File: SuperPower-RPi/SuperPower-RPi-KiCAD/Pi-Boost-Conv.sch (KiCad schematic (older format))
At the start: 22 parts, among them U1 TPS61088

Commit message: Part Meta-data updates continued.
(cherry picked from commit d0ad2c93dfb1e315a7dc98683a53ed7dcb5f49ff)
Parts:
- U1: Digi-Key PN (none) -> 296-43620-1-ND; Mfg (none) -> Texas Instruments; Mfg PN (none) -> TPS61088RHLR
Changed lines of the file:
@@
 F 2 "" H 5550 3250 50  0001 C CNN
 F 3 "https://www.ti.com/lit/ds/symlink/tps61088.pdf?ts=1601341027862" H 5550 3250 50  0001 C CNN
+F 4 "296-43620-1-ND" H 5450 3900 50  0001 C CNN "Digi-Key PN"
+F 5 "Texas Instruments" H 5450 3900 50  0001 C CNN "Mfg"
+F 6 "TPS61088RHLR" H 5450 3900 50  0001 C CNN "Mfg PN"
 	1    5450 3900
 	1    0    0    -1

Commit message: Added local footprint library, and associated components.
(cherry picked from commit 78b1abfd5fe55b90039e798d35239acda24b0417)
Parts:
- C13: footprint (none) -> Capacitor_SMD:C_0603_1608Metric
- L1: Mfg (none) -> FIX FOOTPRINT
- R4: footprint (none) -> Resistor_SMD:R_0603_1608Metric
- U1: footprint (none) -> SuperPower-RPi-KiCAD:TI_VQFN_3.5x4.5mm
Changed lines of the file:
@@
 F 2 "" H 3900 3400 50  0001 C CNN
 F 3 "~" H 3900 3400 50  0001 C CNN
+F 4 "FIX FOOTPRINT" H 3900 3400 50  0001 C CNN "Mfg"
 	1    3900 3400
 	0    -1   -1   0
@@
 F 0 "R4" H 7100 4250 50  0000 C CNN
 F 1 "R" H 7100 4350 50  0000 C CNN
-F 2 "" V 6930 4300 50  0001 C CNN
+F 2 "Resistor_SMD:R_0603_1608Metric" V 6930 4300 50  0001 C CNN
 F 3 "~" H 7000 4300 50  0001 C CNN
 	1    7000 4300
@@
 F 0 "C13" H 6800 4700 50  0000 C CNN
 F 1 "C" H 6850 4800 50  0000 C CNN
-F 2 "" H 7038 4550 50  0001 C CNN
+F 2 "Capacitor_SMD:C_0603_1608Metric" H 7038 4550 50  0001 C CNN
 F 3 "~" H 7000 4700 50  0001 C CNN
 	1    7000 4700
@@
 F 0 "U1" H 5475 3827 50  0000 C CNN
 F 1 "TPS61088" H 5475 3736 50  0000 C CNN
-F 2 "" H 5550 3250 50  0001 C CNN
+F 2 "SuperPower-RPi-KiCAD:TI_VQFN_3.5x4.5mm" H 5550 3250 50  0001 C CNN
 F 3 "https://www.ti.com/lit/ds/symlink/tps61088.pdf?ts=1601341027862" H 5550 3250 50  0001 C CNN
 F 4 "296-43620-1-ND" H 5450 3900 50  0001 C CNN "Digi-Key PN"

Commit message: Added temporary footprints and imported into pcb.
(cherry picked from commit a685dfc635e321a03e1c1fd194e70e2193ef2183)
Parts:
- L1: footprint (none) -> Inductor_SMD:L_Vishay_IHLP-2525
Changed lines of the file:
@@
 F 0 "L1" V 4090 3400 50  0000 C CNN
 F 1 "4.7uH" V 3999 3400 50  0000 C CNN
-F 2 "" H 3900 3400 50  0001 C CNN
+F 2 "Inductor_SMD:L_Vishay_IHLP-2525" H 3900 3400 50  0001 C CNN
 F 3 "~" H 3900 3400 50  0001 C CNN
 F 4 "FIX FOOTPRINT" H 3900 3400 50  0001 C CNN "Mfg"

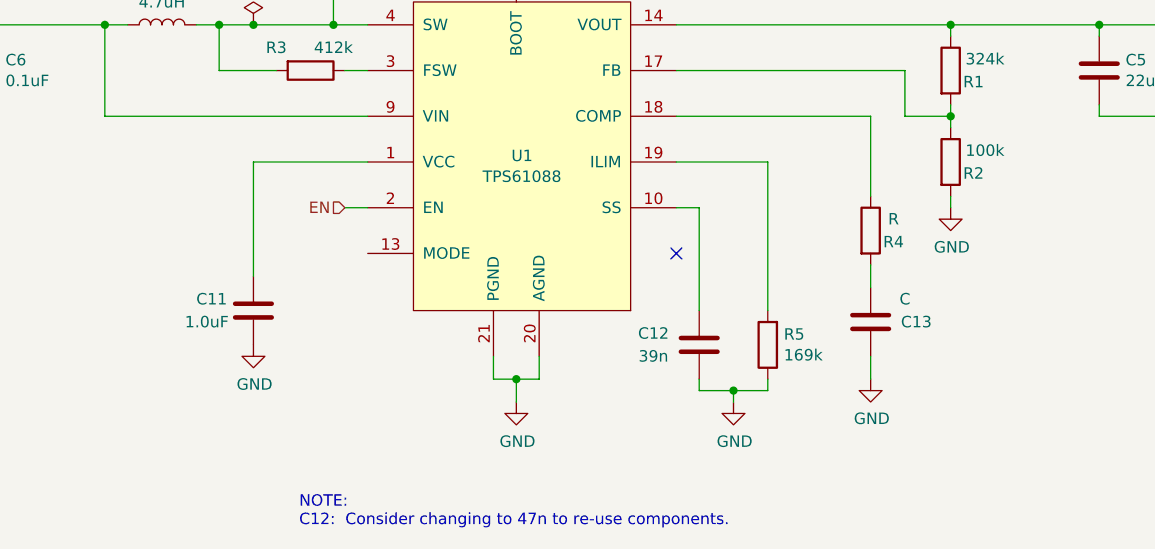
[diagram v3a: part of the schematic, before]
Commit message: PCB Updates.
Added new components, and did some arranging.
Updates TPS61088 and bq25895 footprints to use 0.3mm vias.  PCBWay's minimum via size is 0.3mm.
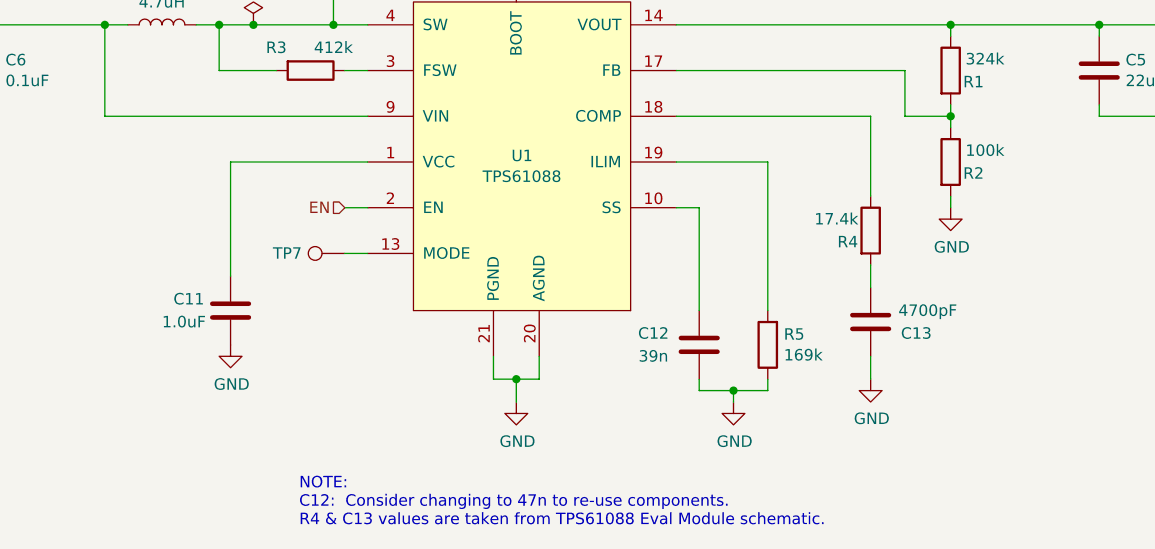
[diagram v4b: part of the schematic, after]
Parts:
- added TP7: DNP, TestPoint:TestPoint_Pad_1.0x1.0mm, symbol Connector:TestPoint
- C13: value C -> 4700pF
- R4: value R -> 17.4k
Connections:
- net at U1.13 (MODE): now also TP7.1
- no-connect marks 1 -> 0
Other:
- note added: "NOTE:\nC12: Consider changing to 47n to re-use components.\nR4 & C13 values are taken from TPS61088 Eval Module schematic."
- note removed: "NOTE:\nC12: Consider changing to 47n to re-use components."
- moved on the sheet: C11

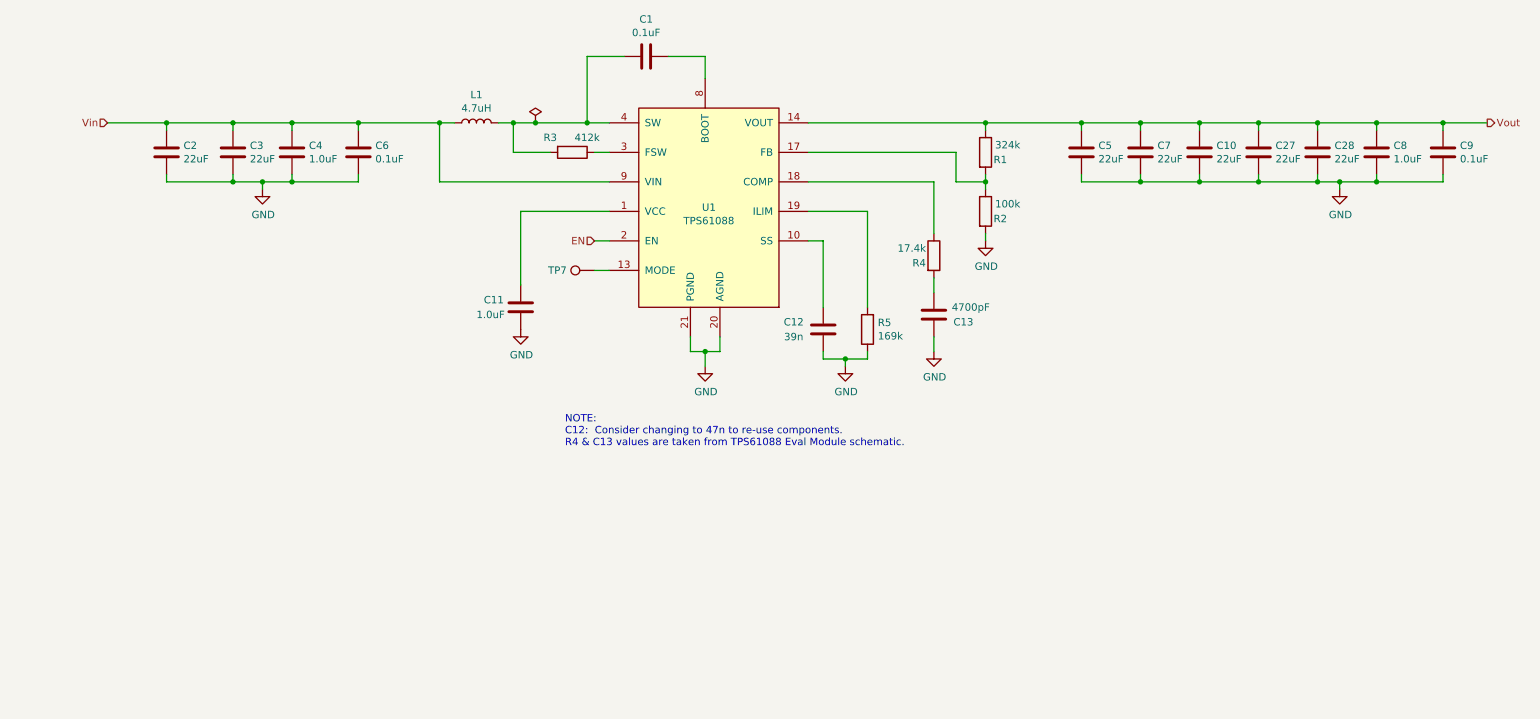
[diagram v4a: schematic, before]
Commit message: Changed Boost Converter passives to the values included in the eval kit.
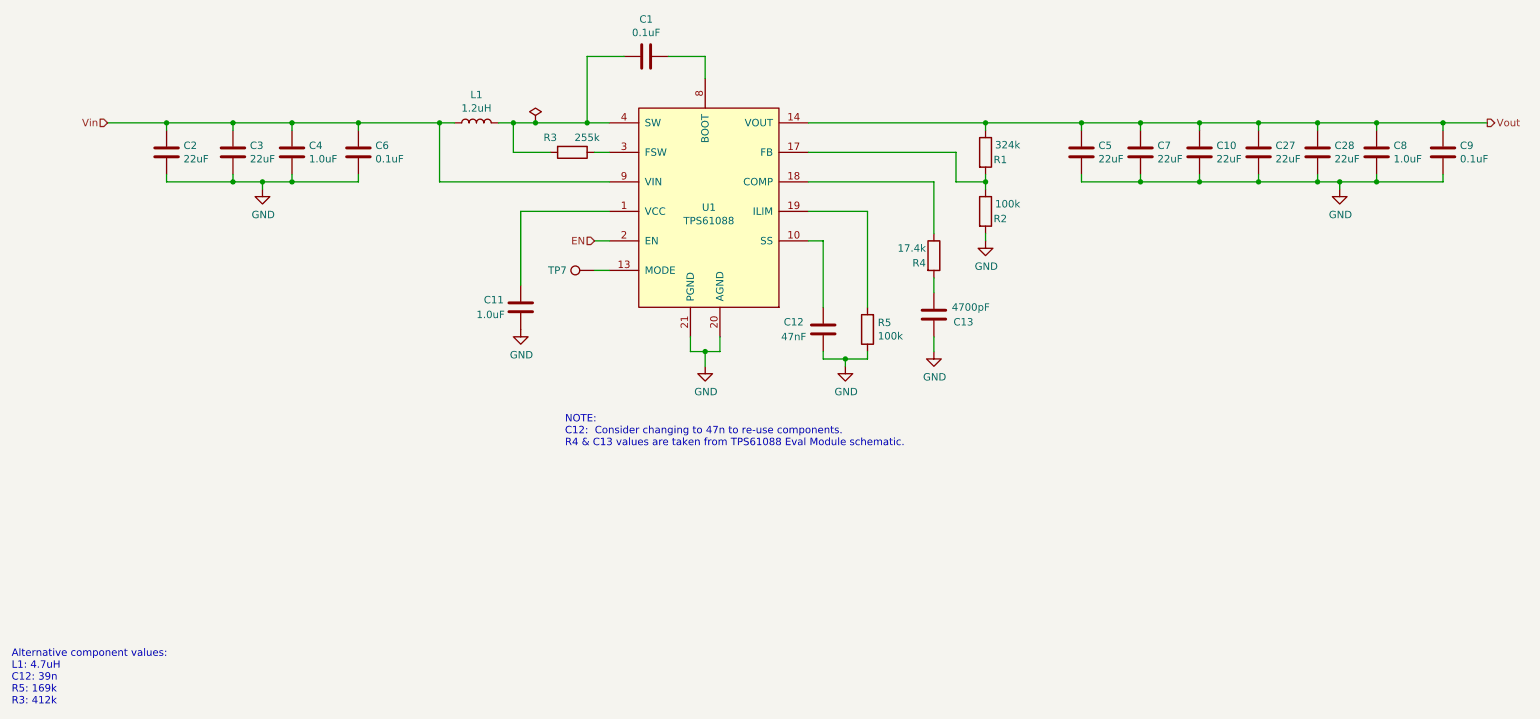
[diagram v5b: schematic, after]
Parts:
- C12: value 39n -> 47nF; footprint Capacitor_SMD:C_0603_1608Metric -> Capacitor_SMD:C_0402_1005Metric; Digi-Key PN (none) -> 490-3254-1-ND; Mfg (none) -> Murata; Mfg PN (none) -> GRM155R71E473KA88D
- C13: footprint Capacitor_SMD:C_0603_1608Metric -> Capacitor_SMD:C_0402_1005Metric
- L1: value 4.7uH -> 1.2uH; footprint Inductor_SMD:L_Vishay_IHLP-2525 -> SuperPower-RPi-KiCAD:L_Sumida_CDMC8D28_9.5x8.7mm; Digi-Key PN (none) -> 308-1618-1-ND; Mfg FIX FOOTPRINT -> Sumida; Mfg PN (none) -> CDMC8D28NP-1R2MC
- R1: footprint Resistor_SMD:R_0603_1608Metric -> Resistor_SMD:R_0402_1005Metric
- R2: footprint Resistor_SMD:R_0603_1608Metric -> Resistor_SMD:R_0402_1005Metric; Digi-Key PN 311-100KHRCT-ND -> (none); Mfg Yageo -> (none); Mfg PN RC0603FR-07100KL -> (none)
- R3: value 412k -> 255k
- R5: value 169k -> 100k
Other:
- note added: "Alternative component values:\nL1: 4.7uH\nC12: 39n\nR5: 169k\nR3: 412k"
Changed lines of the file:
@@
 P 3900 3400
 F 0 "L1" V 4090 3400 50  0000 C CNN
-F 1 "4.7uH" V 3999 3400 50  0000 C CNN
-F 2 "Inductor_SMD:L_Vishay_IHLP-2525" H 3900 3400 50  0001 C CNN
-F 3 "~" H 3900 3400 50  0001 C CNN
-F 4 "FIX FOOTPRINT" H 3900 3400 50  0001 C CNN "Mfg"
+F 1 "1.2uH" V 3999 3400 50  0000 C CNN
+F 2 "SuperPower-RPi-KiCAD:L_Sumida_CDMC8D28_9.5x8.7mm" H 3900 3400 50  0001 C CNN
+F 3 "http://products.sumida.com/products/pdf/CDMC8D28.pdf" H 3900 3400 50  0001 C CNN
+F 4 "Sumida" H 3900 3400 50  0001 C CNN "Mfg"
+F 5 "CDMC8D28NP-1R2MC" H 3900 3400 50  0001 C CNN "Mfg PN"
+F 6 "308-1618-1-ND" H 3900 3400 50  0001 C CNN "Digi-Key PN"
 	1    3900 3400
 	0    -1   -1   0
@@
 F 0 "C13" H 6800 4650 50  0000 C CNN
 F 1 "4700pF" H 6750 4750 50  0000 C CNN
-F 2 "Capacitor_SMD:C_0603_1608Metric" H 7038 4550 50  0001 C CNN
+F 2 "Capacitor_SMD:C_0402_1005Metric" H 7038 4550 50  0001 C CNN
 F 3 "~" H 7000 4700 50  0001 C CNN
 	1    7000 4700
@@
 F 0 "R2" H 7450 3950 50  0000 C CNN
 F 1 "100k" H 7500 4050 50  0000 C CNN
-F 2 "Resistor_SMD:R_0603_1608Metric" V 7280 4000 50  0001 C CNN
+F 2 "Resistor_SMD:R_0402_1005Metric" V 7280 4000 50  0001 C CNN
 F 3 "~" H 7350 4000 50  0001 C CNN
-F 4 "311-100KHRCT-ND" H 7350 4000 50  0001 C CNN "Digi-Key PN"
-F 5 "Yageo" H 7350 4000 50  0001 C CNN "Mfg"
-F 6 "RC0603FR-07100KL" H 7350 4000 50  0001 C CNN "Mfg PN"
 	1    7350 4000
 	1    0    0    -1
@@
 Wire Wire Line
 	3650 3800 4800 3800
-$Comp
-L Device:C C11
-U 1 1 5F73E11E
-P 4200 4650
-F 0 "C11" H 3950 4700 50  0000 L CNN
-F 1 "1.0uF" H 3900 4600 50  0000 L CNN
-F 2 "Capacitor_SMD:C_0603_1608Metric" H 4238 4500 50  0001 C CNN
-F 3 "~" H 4200 4650 50  0001 C CNN
-F 4 "1276-1184-1-ND" H 4200 4650 50  0001 C CNN "Digi-Key PN"
-F 5 "Samsung" H 4200 4650 50  0001 C CNN "Mfg"
-F 6 "CL10B105KA8NNNC" H 4200 4650 50  0001 C CNN "Mfg PN"
-	1    4200 4650
-	1    0    0    -1
-$EndComp
 Wire Wire Line
 	4800 4200 4700 4200
@@
 Wire Wire Line
 	6550 4950 6550 5000
-$Comp
-L Device:R R5
-U 1 1 5F745204
-P 6550 4800
-F 0 "R5" H 6480 4754 50  0000 R CNN
-F 1 "169k" H 6480 4845 50  0000 R CNN
-F 2 "Resistor_SMD:R_0603_1608Metric" V 6480 4800 50  0001 C CNN
-F 3 "~" H 6550 4800 50  0001 C CNN
-	1    6550 4800
-	-1   0    0    1
-$EndComp
 $Comp
 L power:GND #PWR06
@@
 	1    0    0    -1
 $EndComp
-$Comp
-L Device:C C12
-U 1 1 5F7402E9
-P 6250 4800
-F 0 "C12" H 6050 4750 50  0000 C CNN
-F 1 "39n" H 6050 4850 50  0000 C CNN
-F 2 "Capacitor_SMD:C_0603_1608Metric" H 6288 4650 50  0001 C CNN
-F 3 "~" H 6250 4800 50  0001 C CNN
-	1    6250 4800
-	1    0    0    1
-$EndComp
 Wire Wire Line
 	7000 3800 6150 3800
@@
 Wire Wire Line
 	4400 3600 4150 3600
-$Comp
-L Device:R R3
-U 1 1 5F73B183
-P 4550 3600
-F 0 "R3" V 4450 3450 50  0000 C CNN
-F 1 "412k" V 4450 3700 50  0000 C CNN
-F 2 "Resistor_SMD:R_0603_1608Metric" V 4480 3600 50  0001 C CNN
-F 3 "~" H 4550 3600 50  0001 C CNN
-	1    4550 3600
-	0    1    1    0
-$EndComp
 Wire Wire Line
 	6150 3400 7350 3400
@@
 F 0 "R1" H 7450 3550 50  0000 C CNN
 F 1 "324k" H 7500 3650 50  0000 C CNN
-F 2 "Resistor_SMD:R_0603_1608Metric" V 7280 3600 50  0001 C CNN
+F 2 "Resistor_SMD:R_0402_1005Metric" V 7280 3600 50  0001 C CNN
 F 3 "~" H 7350 3600 50  0001 C CNN
 	1    7350 3600
@@
 	1    0    0    -1
 $EndComp
+$Comp
+L Device:C C11
+U 1 1 5F73E11E
+P 4200 4650
+F 0 "C11" H 3950 4700 50  0000 L CNN
+F 1 "1.0uF" H 3900 4600 50  0000 L CNN
+F 2 "Capacitor_SMD:C_0603_1608Metric" H 4238 4500 50  0001 C CNN
+F 3 "~" H 4200 4650 50  0001 C CNN
+F 4 "1276-1184-1-ND" H 4200 4650 50  0001 C CNN "Digi-Key PN"
+F 5 "Samsung" H 4200 4650 50  0001 C CNN "Mfg"
+F 6 "CL10B105KA8NNNC" H 4200 4650 50  0001 C CNN "Mfg PN"
+	1    4200 4650
+	1    0    0    -1
+$EndComp
+$Comp
+L Device:R R3
+U 1 1 5F73B183
+P 4550 3600
+F 0 "R3" V 4450 3450 50  0000 C CNN
+F 1 "255k" V 4450 3700 50  0000 C CNN
+F 2 "Resistor_SMD:R_0603_1608Metric" V 4480 3600 50  0001 C CNN
+F 3 "~" H 4550 3600 50  0001 C CNN
+	1    4550 3600
+	0    1    1    0
+$EndComp
+$Comp
+L Device:C C12
+U 1 1 5F7402E9
+P 6250 4800
+F 0 "C12" H 6050 4750 50  0000 C CNN
+F 1 "47nF" H 6050 4850 50  0000 C CNN
+F 2 "Capacitor_SMD:C_0402_1005Metric" H 6288 4650 50  0001 C CNN
+F 3 "https://search.murata.co.jp/Ceramy/image/img/A01X/G101/ENG/GRM155R71E473KA88-01.pdf" H 6250 4800 50  0001 C CNN
+F 4 "Murata" H 6250 4800 50  0001 C CNN "Mfg"
+F 5 "GRM155R71E473KA88D" H 6250 4800 50  0001 C CNN "Mfg PN"
+F 6 "490-3254-1-ND" H 6250 4800 50  0001 C CNN "Digi-Key PN"
+	1    6250 4800
+	1    0    0    1
+$EndComp
+$Comp
+L Device:R R5
+U 1 1 5F745204
+P 6550 4800
+F 0 "R5" H 6480 4754 50  0000 R CNN
+F 1 "100k" H 6480 4845 50  0000 R CNN
+F 2 "Resistor_SMD:R_0603_1608Metric" V 6480 4800 50  0001 C CNN
+F 3 "~" H 6550 4800 50  0001 C CNN
+	1    6550 4800
+	-1   0    0    1
+$EndComp
+Text Notes 750  7350 0    50   ~ 0
+Alternative component values:\nL1: 4.7uH\nC12: 39n\nR5: 169k\nR3: 412k
 $EndSCHEMATC

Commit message: Changed some passives to 0402 and added some part meta-data.
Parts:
- C1, C6, C9: footprint Capacitor_SMD:C_0603_1608Metric -> Capacitor_SMD:C_0402_1005Metric
- C13: Digi-Key PN (none) -> 311-1039-1-ND; Mfg (none) -> Yageo; Mfg PN (none) -> CC0402KRX7R8BB472
- R4: footprint Resistor_SMD:R_0603_1608Metric -> Resistor_SMD:R_0402_1005Metric
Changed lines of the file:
@@
 F 1 "4700pF" H 6750 4750 50  0000 C CNN
 F 2 "Capacitor_SMD:C_0402_1005Metric" H 7038 4550 50  0001 C CNN
-F 3 "~" H 7000 4700 50  0001 C CNN
+F 3 "https://www.yageo.com/upload/media/product/productsearch/datasheet/mlcc/UPY-GPHC_X7R_6.3V-to-50V_18.pdf" H 7000 4700 50  0001 C CNN
+F 4 "Yageo" H 7000 4700 50  0001 C CNN "Mfg"
+F 5 "CC0402KRX7R8BB472" H 7000 4700 50  0001 C CNN "Mfg PN"
+F 6 "311-1039-1-ND" H 7000 4700 50  0001 C CNN "Digi-Key PN"
 	1    7000 4700
 	-1   0    0    -1
@@
 F 0 "C9" H 10565 3646 50  0000 L CNN
 F 1 "0.1uF" H 10565 3555 50  0000 L CNN
-F 2 "Capacitor_SMD:C_0603_1608Metric" H 10488 3450 50  0001 C CNN
+F 2 "Capacitor_SMD:C_0402_1005Metric" H 10488 3450 50  0001 C CNN
 F 3 "~" H 10450 3600 50  0001 C CNN
 	1    10450 3600
@@
 F 0 "C1" V 4798 2950 50  0000 C CNN
 F 1 "0.1uF" V 4889 2950 50  0000 C CNN
-F 2 "Capacitor_SMD:C_0603_1608Metric" H 5088 2800 50  0001 C CNN
+F 2 "Capacitor_SMD:C_0402_1005Metric" H 5088 2800 50  0001 C CNN
 F 3 "~" H 5050 2950 50  0001 C CNN
 	1    5050 2950
@@
 F 0 "C6" H 3215 3646 50  0000 L CNN
 F 1 "0.1uF" H 3215 3555 50  0000 L CNN
-F 2 "Capacitor_SMD:C_0603_1608Metric" H 3138 3450 50  0001 C CNN
+F 2 "Capacitor_SMD:C_0402_1005Metric" H 3138 3450 50  0001 C CNN
 F 3 "~" H 3100 3600 50  0001 C CNN
 	1    3100 3600
@@
 F 0 "R4" H 6900 4250 50  0000 C CNN
 F 1 "17.4k" H 6850 4350 50  0000 C CNN
-F 2 "Resistor_SMD:R_0603_1608Metric" V 6930 4300 50  0001 C CNN
+F 2 "Resistor_SMD:R_0402_1005Metric" V 6930 4300 50  0001 C CNN
 F 3 "~" H 7000 4300 50  0001 C CNN
 	1    7000 4300

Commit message: Updated meta-data.
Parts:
- TP7: Mfg (none) -> DNP
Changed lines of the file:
@@
 F 2 "TestPoint:TestPoint_Pad_1.0x1.0mm" H 4900 4400 50  0001 C CNN
 F 3 "~" H 4900 4400 50  0001 C CNN
+F 4 "DNP" H 4700 4400 50  0001 C CNN "Mfg"
 	1    4700 4400
 	0    -1   -1   0

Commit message: Updated 1uF caps to 0402 package.
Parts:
- C11, C4, C8: footprint Capacitor_SMD:C_0603_1608Metric -> Capacitor_SMD:C_0402_1005Metric; Digi-Key PN 1276-1184-1-ND -> 490-10017-1-ND; Mfg Samsung -> Murata Electronics; Mfg PN CL10B105KA8NNNC -> GRM155R61E105KA12D
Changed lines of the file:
@@
 F 0 "C4" H 2765 3646 50  0000 L CNN
 F 1 "1.0uF" H 2765 3555 50  0000 L CNN
-F 2 "Capacitor_SMD:C_0603_1608Metric" H 2688 3450 50  0001 C CNN
+F 2 "Capacitor_SMD:C_0402_1005Metric" H 2688 3450 50  0001 C CNN
 F 3 "~" H 2650 3600 50  0001 C CNN
-F 4 "1276-1184-1-ND" H 2650 3600 50  0001 C CNN "Digi-Key PN"
-F 5 "Samsung" H 2650 3600 50  0001 C CNN "Mfg"
-F 6 "CL10B105KA8NNNC" H 2650 3600 50  0001 C CNN "Mfg PN"
+F 4 "490-10017-1-ND" H 2650 3600 50  0001 C CNN "Digi-Key PN"
+F 5 "Murata Electronics" H 2650 3600 50  0001 C CNN "Mfg"
+F 6 "GRM155R61E105KA12D" H 2650 3600 50  0001 C CNN "Mfg PN"
 	1    2650 3600
 	1    0    0    -1
@@
 F 0 "C8" H 10115 3646 50  0000 L CNN
 F 1 "1.0uF" H 10115 3555 50  0000 L CNN
-F 2 "Capacitor_SMD:C_0603_1608Metric" H 10038 3450 50  0001 C CNN
+F 2 "Capacitor_SMD:C_0402_1005Metric" H 10038 3450 50  0001 C CNN
 F 3 "~" H 10000 3600 50  0001 C CNN
-F 4 "1276-1184-1-ND" H 10000 3600 50  0001 C CNN "Digi-Key PN"
-F 5 "Samsung" H 10000 3600 50  0001 C CNN "Mfg"
-F 6 "CL10B105KA8NNNC" H 10000 3600 50  0001 C CNN "Mfg PN"
+F 4 "490-10017-1-ND" H 10000 3600 50  0001 C CNN "Digi-Key PN"
+F 5 "Murata Electronics" H 10000 3600 50  0001 C CNN "Mfg"
+F 6 "GRM155R61E105KA12D" H 10000 3600 50  0001 C CNN "Mfg PN"
 	1    10000 3600
 	1    0    0    -1
@@
 F 0 "C11" H 3950 4700 50  0000 L CNN
 F 1 "1.0uF" H 3900 4600 50  0000 L CNN
-F 2 "Capacitor_SMD:C_0603_1608Metric" H 4238 4500 50  0001 C CNN
+F 2 "Capacitor_SMD:C_0402_1005Metric" H 4238 4500 50  0001 C CNN
 F 3 "~" H 4200 4650 50  0001 C CNN
-F 4 "1276-1184-1-ND" H 4200 4650 50  0001 C CNN "Digi-Key PN"
-F 5 "Samsung" H 4200 4650 50  0001 C CNN "Mfg"
-F 6 "CL10B105KA8NNNC" H 4200 4650 50  0001 C CNN "Mfg PN"
+F 4 "490-10017-1-ND" H 4200 4650 50  0001 C CNN "Digi-Key PN"
+F 5 "Murata Electronics" H 4200 4650 50  0001 C CNN "Mfg"
+F 6 "GRM155R61E105KA12D" H 4200 4650 50  0001 C CNN "Mfg PN"
 	1    4200 4650
 	1    0    0    -1
